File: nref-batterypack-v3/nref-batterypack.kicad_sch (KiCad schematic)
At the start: 91 parts, among them J0 C1-, J1 C1-, J2 C2+, J3 C3-, J4 C4+, J5 PACK_CONN, J6 BACK_CONN, Q1 BC817, Q2 BC817, Q3 BC817, Q4 BC817, Q5 AO3401A, Q7 AO3401A, Q8 Q_Dual_NMOS_Picostar_CSD87501L, U1 BQ76922

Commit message: PCBs: add various notes
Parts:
- D1: LCSC (none) -> C95171; Preorder (none) -> n
- D10, D11, D12, D13, D14, D15, D16, D8: LCSC (none) -> C134385; Preorder (none) -> y
- D17, D18, D19, D9: LCSC (none) -> C130719; Preorder (none) -> n
- D2, D3, D4, D5: LCSC (none) -> C391400; Preorder (none) -> y
- J1, J3: Preorder (none) -> TODO
- J2, J4: LCSC (none) -> C20777560; MPN S174146R -> 2036-3-57-15-00-00-03-0; Manufacturer Harwin -> Mill-Max; Preorder (none) -> y
- J5: LCSC (none) -> C160393; Preorder (none) -> n
- J6: LCSC (none) -> C160402; Preorder (none) -> n
- Q1, Q2, Q3, Q4: LCSC (none) -> C12766; Preorder (none) -> n (clone)
- Q5, Q7: LCSC (none) -> C15127; Preorder (none) -> n
- Q8: LCSC (none) -> C2841784; Preorder (none) -> y, global sourcing
- R1, R2, R3, R4: LCSC (none) -> C4059300; Preorder (none) -> y-replace?
- R19, R20, R23, R24: LCSC (none) -> C2765609; Preorder (none) -> replace with basic
- R26: LCSC (none) -> C2086089; Preorder (none) -> y-replace?
- R5: LCSC (none) -> C20349383; Preorder (none) -> y-replace?
- TH1, TH3, TH4: LCSC (none) -> C24890359; Preorder (none) -> y-replace?
- TH2: LCSC (none) -> C24890359; Preorder (none) -> y-replace?; now not fitted
- U1: LCSC (none) -> C33651534; Preorder (none) -> y, global sourcing
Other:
- note added: "4mA"
- note added: "TODO: remove TH2 for full shutdown ability"

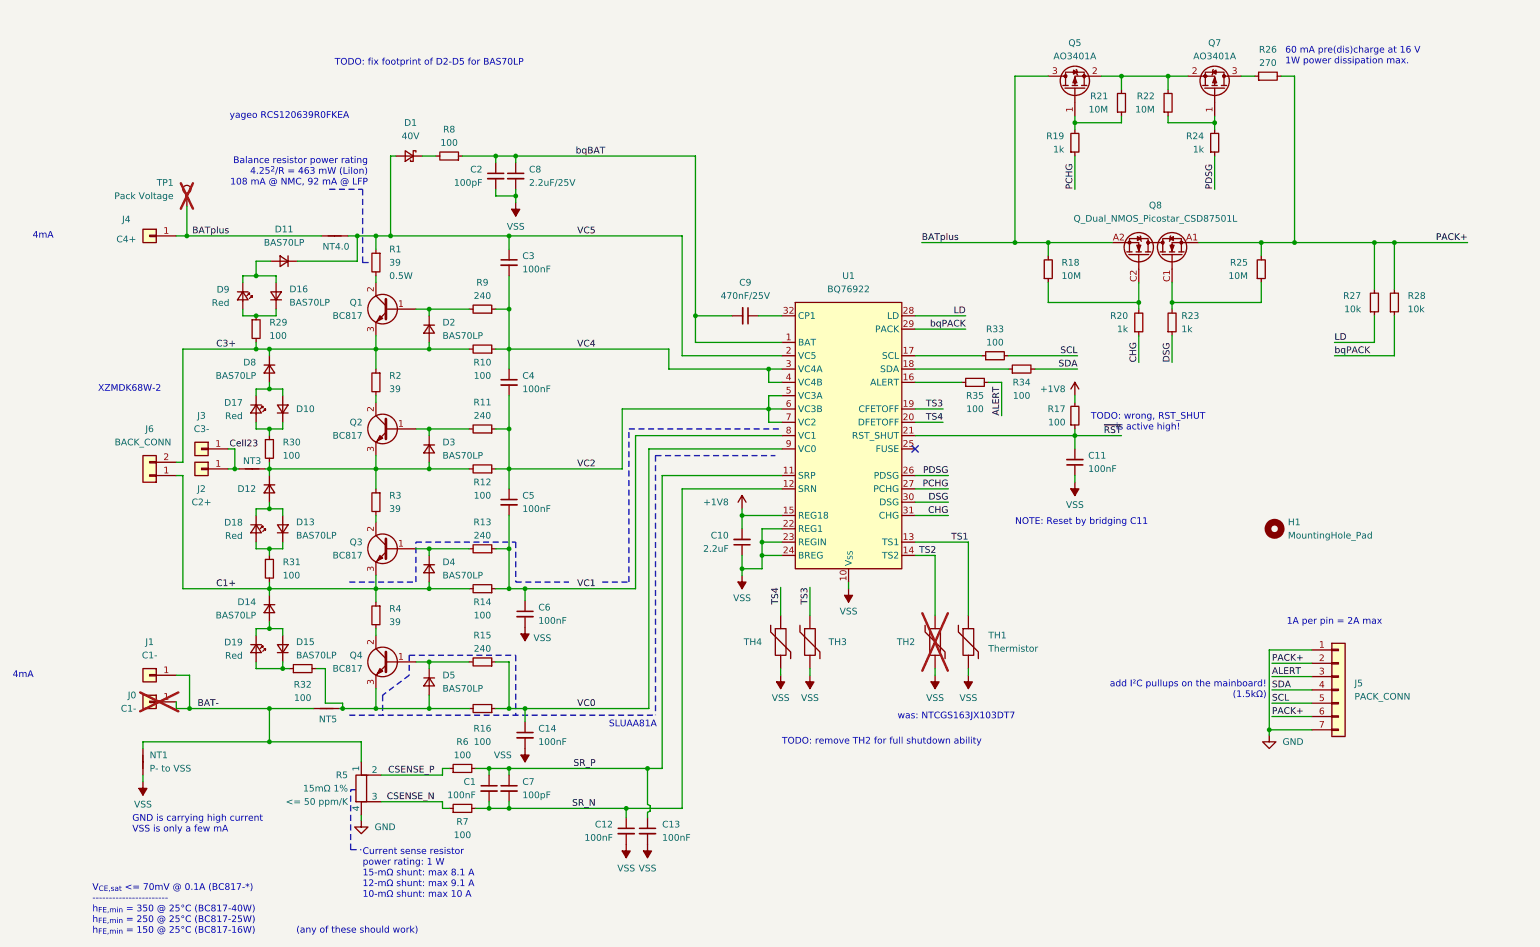
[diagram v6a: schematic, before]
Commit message: batterypack back/front: polishing for production
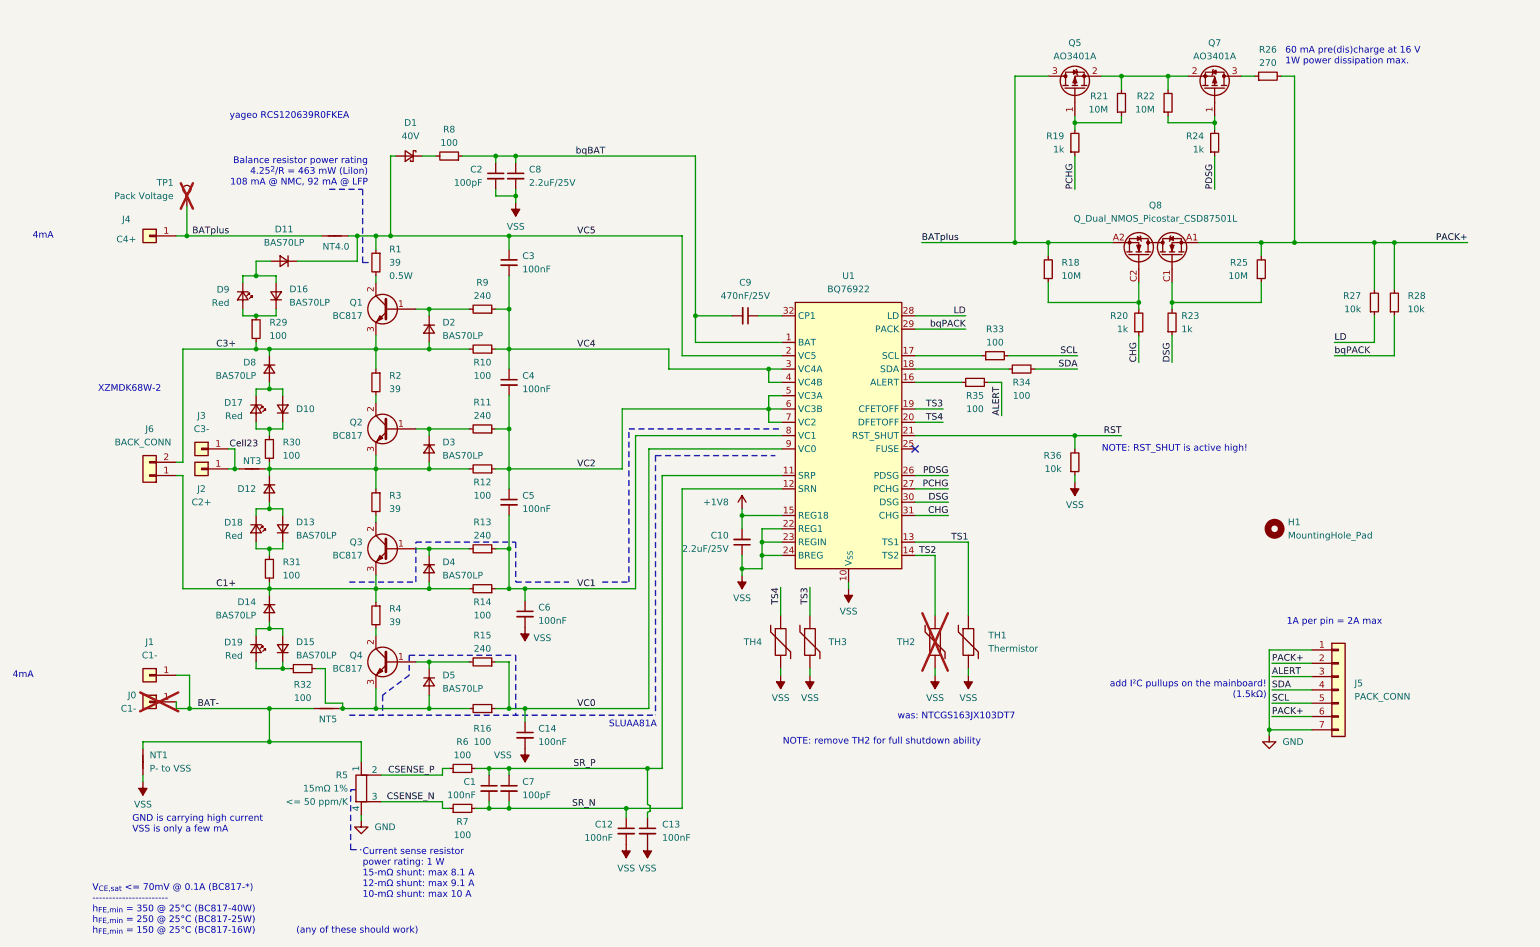
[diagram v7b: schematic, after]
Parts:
- removed C11: 100nF, Capacitor_SMD:C_0402_1005Metric, symbol Device:C_Small
- removed R17: 100, Resistor_SMD:R_0402_1005Metric, symbol Device:R_Small
- added R36: 10k, Resistor_SMD:R_0402_1005Metric, symbol Device:R_Small
- C1, C12, C13, C14, C3, C4, C5, C6: LCSC (none) -> C1525; MPN GRM155R71C104KA88J -> CL05B104KO5NNNC; Manufacturer Murata -> Samsung
- C10: value 2.2uF -> 2.2uF/25V; LCSC (none) -> C72203
- C2, C7: LCSC (none) -> C1546; MPN GRM1555C1H101JA01D -> 0402CG101J500NT; Manufacturer Murata -> FH
- C8: LCSC (none) -> C72203; MPN GRM155C81E225ME11D -> GRM155R61E225ME15D
- C9: LCSC (none) -> C92361; MPN GRM155R61H474KE11J -> CL05A474KA5NNNC; Manufacturer Murata -> Samsung
- D10, D11, D12, D13, D14, D15, D16, D8: Preorder y -> n
- D2, D3, D4, D5: footprint Diode_SMD:D_SOD-323F -> Diode_SMD:D_SOD-882; LCSC C391400 -> C134385; MPN BAS70WS_R1_00001 -> BAS70LP-7B; Preorder y -> n
- J1, J3: footprint footprints:S70332002045R -> footprints:MYOUNG_MY-FJ-115; LCSC (none) -> C5457098; MPN S70-332002045R -> MY-FJ-115; Manufacturer Harwin -> MYOUNG; Preorder TODO -> n
- J2, J4: footprint footprints:S174146R -> footprints:Mill-Max_2036-X-57; Preorder y -> y, global sourcing
- R1, R2, R3, R4: LCSC C4059300 -> C5713422; MPN CRGH1206J39R -> FRP1206J390 TS; Manufacturer TE Connextivity -> FOJAN; Preorder y-replace? -> (none)
- R10, R12, R14, R16, R29, R30, R31, R32, R33, R34, R35, R6, R7, R8: LCSC (none) -> C25076; MPN RC0402FR-07100RL -> 0402WGF1000TCE; Manufacturer Yageo -> UNI-ROYAL
- R11, R13, R15, R9: LCSC (none) -> C114755
- R18, R21, R22, R25: LCSC (none) -> C138067
- R19, R20, R23, R24: LCSC C2765609 -> C11702; MPN CQ02WGF1001TCE -> 0402WGF1001TCE; Manufacturer Royalohm -> UNI-ROYAL; Preorder replace with basic -> (none)
- R26: footprint Resistor_SMD:R_0612_1632Metric -> Resistor_SMD:R_1812_4532Metric; LCSC C2086089 -> C49656236; MPN LTR18EZPF2700 -> GR1812J270RT4G00; Manufacturer Rohm -> GiantOhm; Preorder y-replace? -> (none)
- R27, R28: LCSC (none) -> C25744; MPN RC0402JR-0710KL -> 0402WGF1002TCE; Manufacturer Yageo -> UNI-ROYAL
- R5: LCSC C20349383 -> C6142742; MPN L4CA0612LR015FNR -> PE0612FKF070R015L; Manufacturer Littlefuse -> Yageo; Preorder y-replace? -> (none)
- TH1, TH3, TH4: LCSC C24890359 -> C2889040; MPN NTCGS103JX103DT7 -> CMFX 103F3435; Manufacturer TDK -> Nanjing Shiheng; Preorder y-replace? -> n
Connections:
- net VSS: now also R36.1
- net ~{RST} renamed RST
- net RST: now also R36.2
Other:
- note added: "NOTE: RST_SHUT is active high!"
- note added: "NOTE: remove TH2 for full shutdown ability"
- note removed: "NOTE: Reset by bridging C11"
- note removed: "TODO: fix footprint of D2-D5 for BAS70LP"
- note removed: "TODO: remove TH2 for full shutdown ability"
- note removed: "TODO: wrong, RST_SHUT is active high!"
